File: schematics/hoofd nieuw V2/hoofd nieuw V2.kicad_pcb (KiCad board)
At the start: 2 copper layers, 170 x 75 mm, 41 parts, among them J1 Conn_01x04_Pin, J2 Conn_01x02_Pin, J3 SFR02, J4 Conn_01x03_Pin, U1 ATtiny402-SS, U2 BH1750FVI-TR, U3 BH1750FVI-TR, Y1 ECS-2333MV-100-BN-TR

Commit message: zet alles op de juiste plaats
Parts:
- added H1: MountingHole, MountingHole:MountingHole_3.5mm, F.Cu at (49.8, 49.2)
- added H2: MountingHole, MountingHole:MountingHole_3.5mm, F.Cu at (213.3, 49.8)
- D20: value ~ -> D5V0P4B5LP08
- moved C3 2.50 mm to (164.8, 71.2)
- moved C5 2.50 mm to (104.5, 51.9)
- moved C7 2.50 mm to (85.9, 68.3)
- moved C8 2.50 mm to (170.9, 68.3)
- moved D1 2.50 mm to (104.2, 47.0), turned to -90 degrees
- moved D15 2.50 mm to (161.0, 66.0)
- moved D16 2.50 mm to (180.0, 75.0)
- moved D17 2.50 mm to (187.8, 65.0)
- moved D18 2.50 mm to (178.5, 38.5)
- moved D19 2.50 mm to (157.8, 47.3)
- moved D2 2.50 mm to (83.8, 38.5)
- moved D3 2.50 mm to (74.2, 65.0)
- moved D4 2.50 mm to (83.0, 75.0), turned to 180 degrees
- moved D5 2.50 mm to (102.0, 66.0), turned to 90 degrees
- moved U2 2.50 mm to (89.0, 68.0)
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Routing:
- net +5V: track 325.0 -> 0.00 mm, vias 2 -> 0
- net /SDA: track 128.7 -> 0.00 mm, vias 10 -> 0
- net /SCL: track 120.0 -> 0.00 mm, vias 5 -> 0
- net +3.3V: track 116.3 -> 7.28 mm, vias 2 -> 0
- net Net-(U2-DVI): track 107.3 -> 0.00 mm, vias 6 -> 0
- net Net-(D17-DOUT): track 31.2 -> 0.00 mm
- net Net-(D4-DOUT): track 29.3 -> 0.00 mm
- net Net-(D2-DOUT): track 25.1 -> 0.00 mm
- net Net-(D1-DOUT): track 20.5 -> 0.00 mm
- net Net-(D15-DOUT): track 19.2 -> 0.00 mm
- net Net-(D18-DOUT): track 18.1 -> 0.00 mm
- net Net-(D3-DOUT): track 17.1 -> 0.00 mm
- net Net-(D14-DOUT): track 16.0 -> 0.00 mm
- net Net-(D1-DIN): track 14.6 -> 0.00 mm
- net Net-(D5-DOUT): track 12.7 -> 0.00 mm
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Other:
- board size 170 x 75 mm -> 177.5 x 75 mm

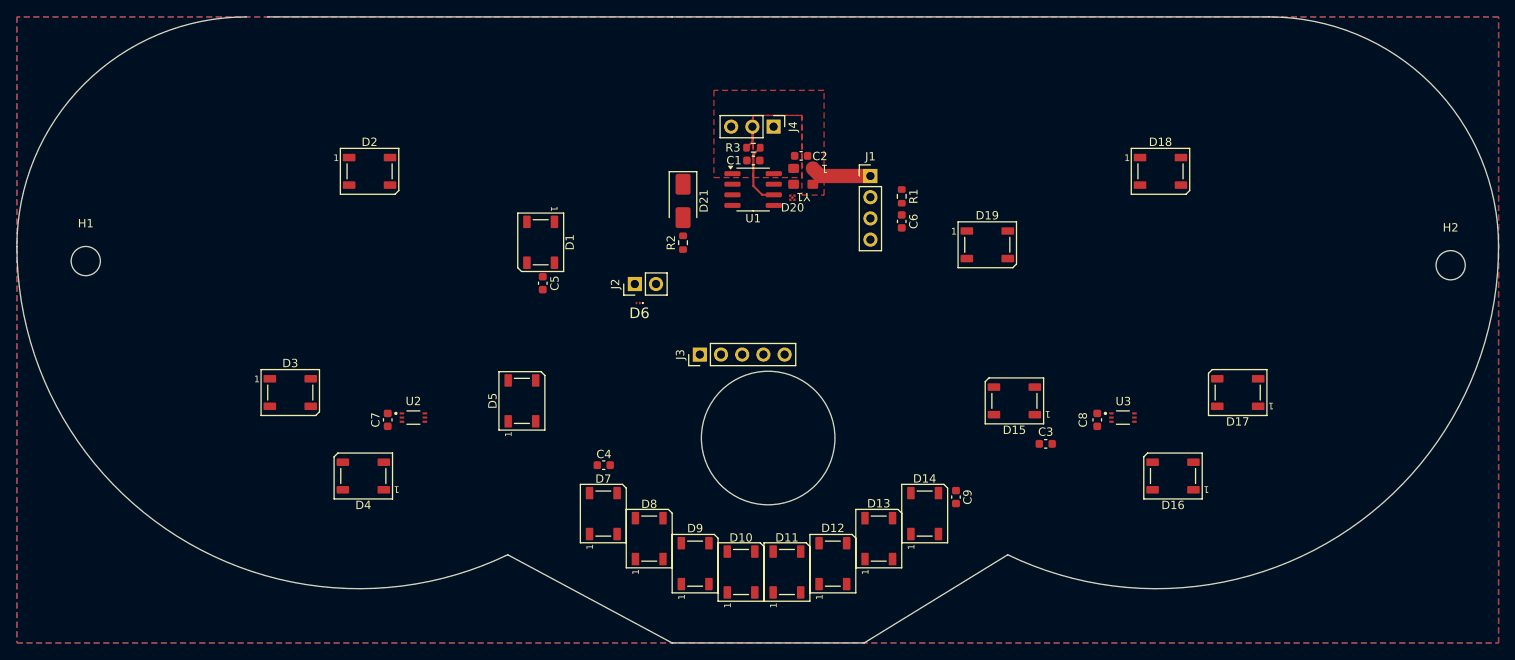
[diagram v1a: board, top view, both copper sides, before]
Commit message: teken al wat van het nieuw hoofd
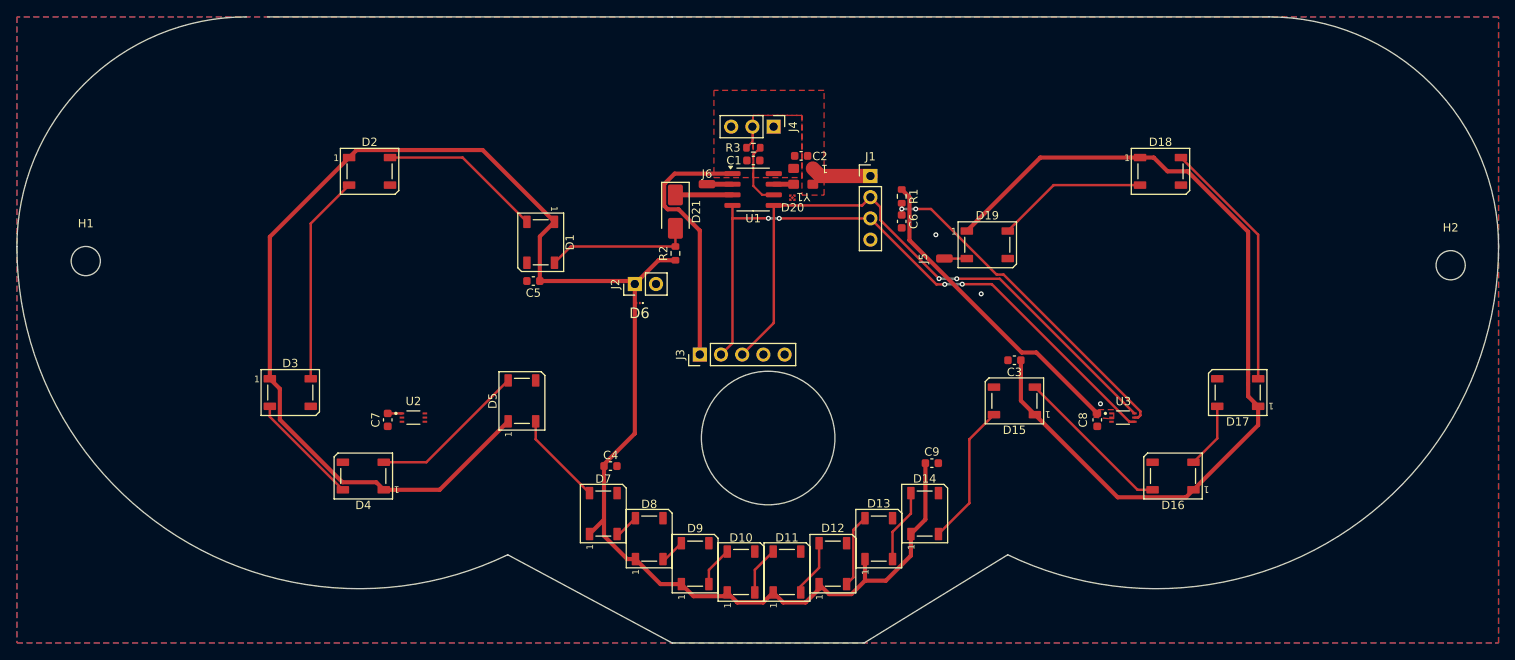
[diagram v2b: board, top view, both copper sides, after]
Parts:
- added J5: Conn_01x01, Connector_Wire:SolderWirePad_1x01_SMD_1x2mm, F.Cu at (152.6, 48.9)
- added J6: Conn_01x01, Connector_Wire:SolderWirePad_1x01_SMD_1x2mm, F.Cu at (124.2, 40.0)
- moved C3 10.7 mm to (161.0, 61.1), turned to 180 degrees
- moved C9 4.99 mm to (151.1, 73.5), turned to 0 degrees
- moved D21 1.57 mm to (120.4, 43.3)
- moved R2 1.57 mm to (120.4, 48.3)
- moved C5 1.16 mm to (103.4, 51.6), turned to 180 degrees
- moved C4 0.82 mm to (112.6, 73.8)
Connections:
- D19 pad 2: unconnected-(D19-DOUT-Pad2) -> Net-(D19-DOUT)
- U1 pad 2: Net-(D21-K) -> Net-(J6-Pin_1)
- U1 pad 3: unconnected-(U1-PA7-Pad3) -> Net-(D21-K)
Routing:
- net +5V: track 0.00 -> 324.0 mm
- net /SDA: track 0.00 -> 76.7 mm, vias 0 -> 4
- net /SCL: track 0.00 -> 74.7 mm, vias 0 -> 2
- net +3.3V: track 7.28 -> 78.2 mm
- net Net-(U2-DVI): track 0.00 -> 41.3 mm, vias 0 -> 2
- net Net-(D17-DOUT): track 0.00 -> 30.3 mm
- net Net-(D2-DOUT): track 0.00 -> 25.1 mm
- net Net-(D1-DOUT): track 0.00 -> 19.6 mm
- net Net-(D15-DOUT): track 0.00 -> 19.2 mm
- net Net-(D4-DOUT): track 0.00 -> 19.0 mm
- net Net-(D18-DOUT): track 0.00 -> 18.1 mm
- net Net-(D1-DIN): track 0.00 -> 17.5 mm
- net Net-(D14-DOUT): track 0.00 -> 17.1 mm
- net Net-(D3-DOUT): track 0.00 -> 13.6 mm
- net Net-(D5-DOUT): track 0.00 -> 11.3 mm
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
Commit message: zet de leds en lichtsensoren op de juisteplaats nieuw hoofd V2
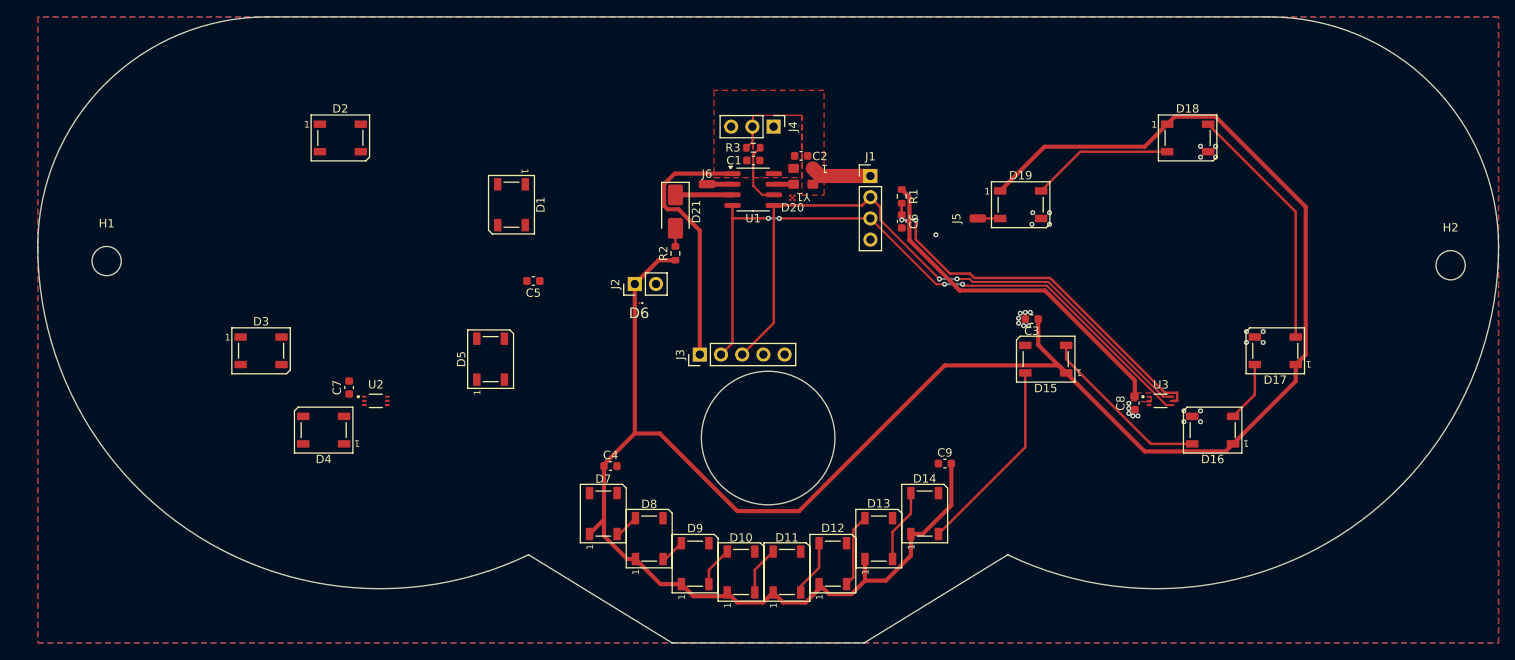
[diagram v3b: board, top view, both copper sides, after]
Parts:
- moved D16 7.27 mm to (184.8, 69.5)
- moved D4 7.27 mm to (78.2, 69.5)
- moved D17 6.73 mm to (192.2, 60.0)
- moved D15 6.25 mm to (164.8, 61.0)
- moved D5 6.25 mm to (98.2, 61.0)
- moved D19 6.25 mm to (161.8, 42.5)
- moved J5 6.25 mm to (156.6, 44.1)
- moved D3 6.10 mm to (70.8, 60.0)
- moved C7 6.03 mm to (81.3, 64.4)
- moved D1 5.70 mm to (100.8, 42.5)
- moved C3 5.35 mm to (163.1, 56.2)
- moved D2 5.32 mm to (80.2, 34.5)
- moved D18 5.15 mm to (181.8, 34.5)
- moved C8 4.92 mm to (175.4, 66.3)
- moved U2 4.92 mm to (84.5, 66.0)
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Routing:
- net +5V: track 324.0 -> 274.2 mm
- net Net-(D2-DOUT): track 25.1 -> 0.00 mm
- net Net-(D1-DOUT): track 19.6 -> 0.00 mm
- net Net-(D4-DOUT): track 19.0 -> 0.00 mm
- net Net-(D1-DIN): track 17.5 -> 2.18 mm
- net Net-(D3-DOUT): track 13.6 -> 0.00 mm
- net Net-(D5-DOUT): track 11.3 -> 0.00 mm
- net Net-(D14-DOUT): track 17.1 -> 23.6 mm
- net Net-(U2-DVI): track 41.3 -> 46.5 mm
- net /SCL: track 74.7 -> 78.3 mm
- net /SDA: track 76.7 -> 80.4 mm
- net +3.3V: track 78.2 -> 81.3 mm
- net Net-(D15-DOUT): track 19.2 -> 21.0 mm
- net Net-(D18-DOUT): track 18.1 -> 17.0 mm
- net Net-(D16-DOUT): track 7.88 -> 7.28 mm
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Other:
- board size 177.5 x 75 mm -> 175 x 75 mm

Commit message: nieuw hoofd V2 is klaar
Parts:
- removed D20: D5V0P4B5LP08, Library:D5V0P4B5LP08
- moved C5 5.43 mm to (99.8, 47.5)
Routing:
- net +5V: track 274.2 -> 399.6 mm
- net Net-(U2-DVI): track 46.5 -> 121.4 mm, vias 2 -> 7
- net +3.3V: track 81.3 -> 141.5 mm, vias 0 -> 2
- net /SCL: track 78.3 -> 124.1 mm, vias 2 -> 6
- net /SDA: track 80.4 -> 123.5 mm, vias 4 -> 8
- net Net-(D2-DOUT): track 0.00 -> 24.1 mm
- net Net-(D4-DOUT): track 0.00 -> 19.8 mm
- net Net-(D1-DOUT): track 0.00 -> 19.4 mm
- net Net-(D1-DIN): track 2.18 -> 20.3 mm
- net Net-(D5-DOUT): track 0.00 -> 17.8 mm
- net Net-(D3-DOUT): track 0.00 -> 12.6 mm
- net GND: vias 29 -> 142
